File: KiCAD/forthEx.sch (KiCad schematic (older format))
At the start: 51 parts, among them CON1 BARREL_JACK 2,1mm, J1 RCA_JACK, J2 RCA_JACK, J3 USB-A_F, J4 miniDIN-6, P1 ICSP, Q1 2N3906, Q2 2N3904, SW1 Power, SW2 reset, U1 LD1117v33, U2 PIC24EP512GP202, U3 25LC1024, U4 23LC1024, X1 8Mhz

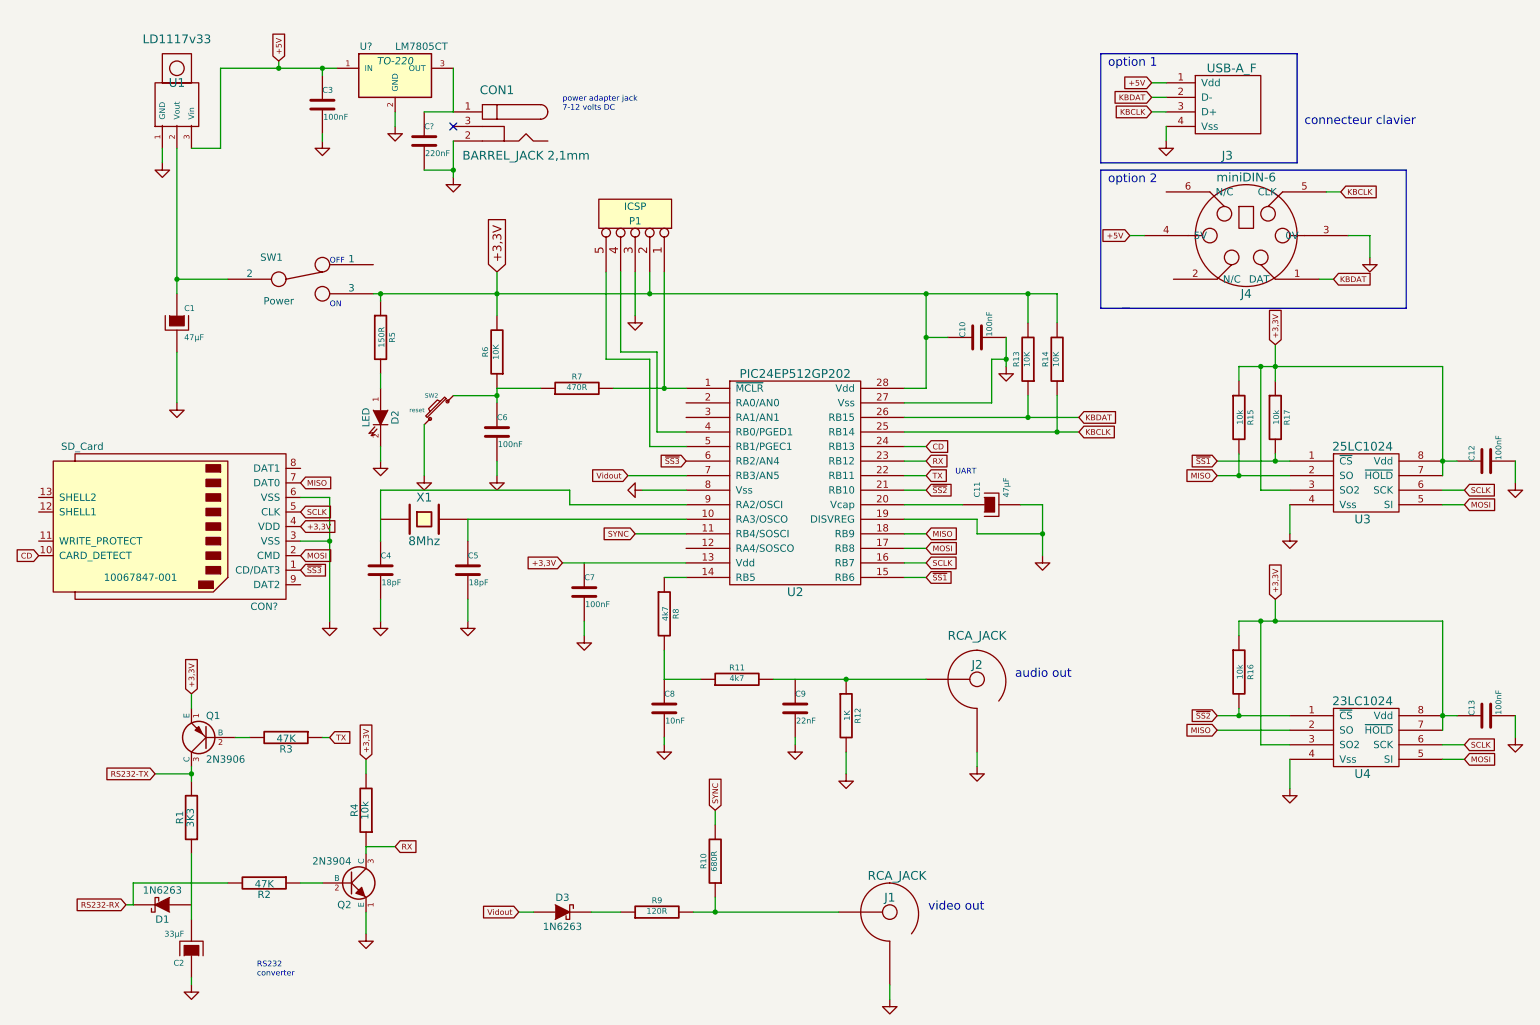
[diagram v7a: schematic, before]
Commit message: ajout kbd_send
ajout commande KCMD_RESET  à procédure initialisation
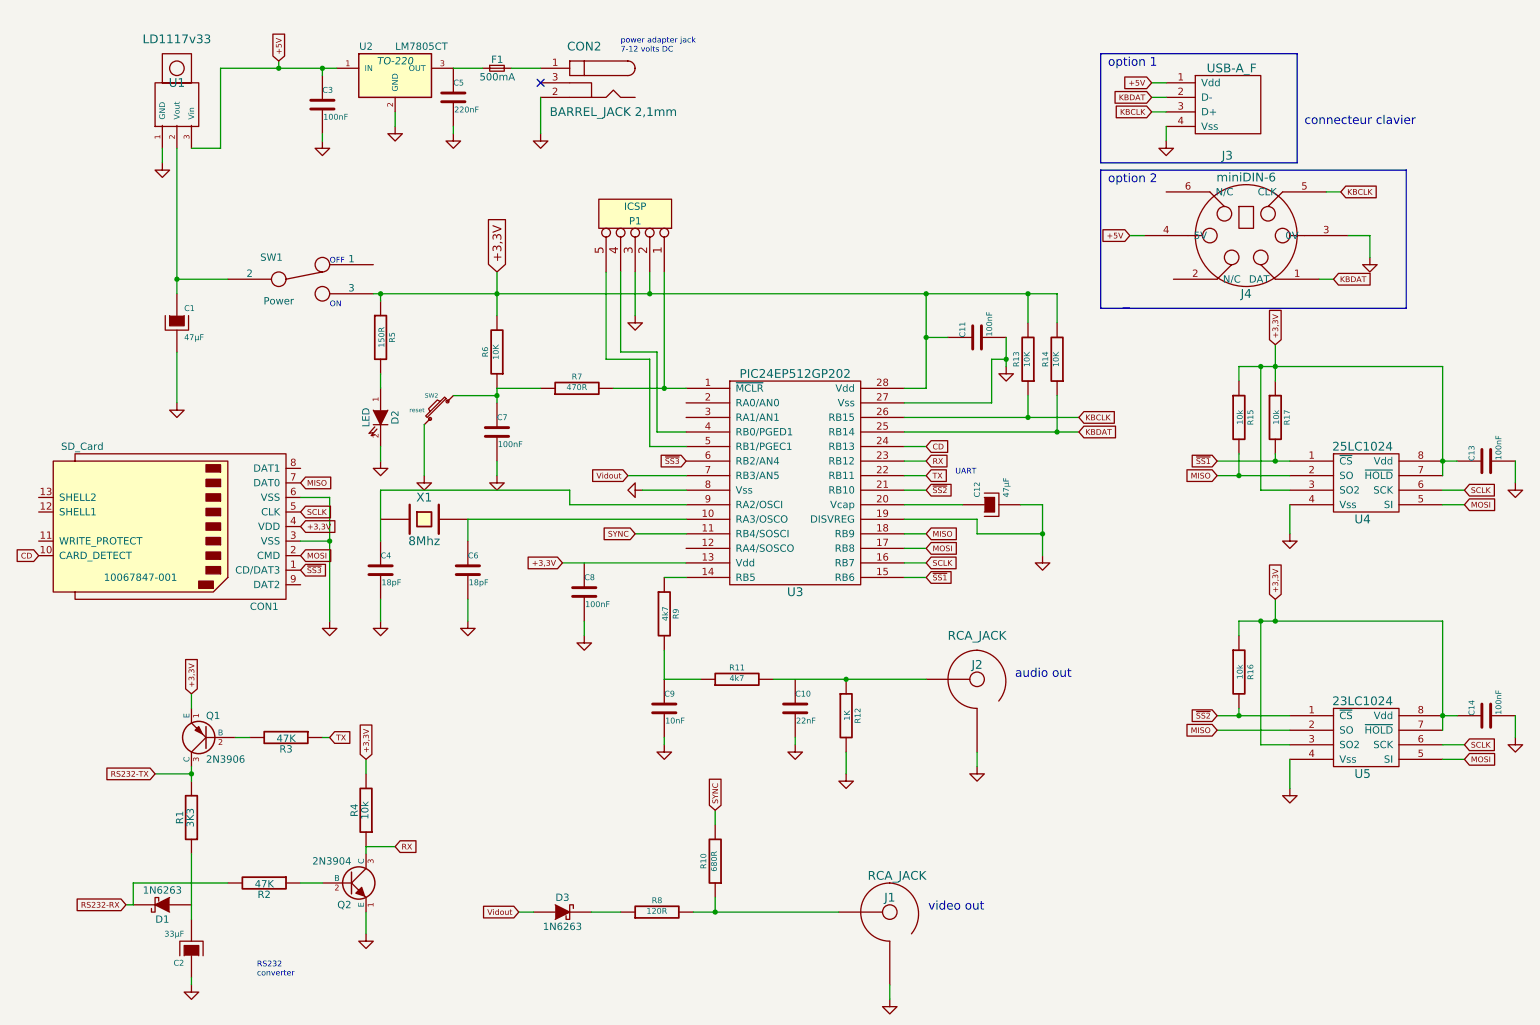
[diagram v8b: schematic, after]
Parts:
- added F1: 500mA, symbol F_Small
- gave numbers to parts that had none: 3
- renumbered C9 to C10, C10 to C11, C11 to C12, C12 to C13, C13 to C14, C5 to C6, C6 to C7, C7 to C8, C8 to C9, CON1 to CON2, R9 to R8, R8 to R9, U2 to U3, U3 to U4, U4 to U5
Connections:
- net KBCLK: now also R13.1, U3.26 (RB15); no longer R14.1, U3.25 (RB14)
- net KBDAT: now also R14.1, U3.25 (RB14); no longer R13.1, U3.26 (RB15)
- net at C5.1, U2.3 (OUT): now also F1.1; no longer CON2.1
- new net: CON2.1, F1.2
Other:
- moved on the sheet: C5, CON2
